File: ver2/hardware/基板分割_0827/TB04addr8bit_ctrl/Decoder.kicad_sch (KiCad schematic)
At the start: 12 parts, among them U701 74LS273, U702 74LS273, U703 28C256, U704 28C256, U705 74LS273, U706 28C256

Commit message: ver2: 3分割で他基板側のICを削除(ctrl 9・alu 15・if 2個)
削除前にまたぎ本数(37/20)で割り当てを検算。kicad-cliのパース通過を確認。

Co-Authored-By: Claude Opus 5 <noreply@anthropic.com>
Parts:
- removed U702: 74LS273, Package_DIP:DIP-20_W7.62mm_Socket, symbol 74xx:74LS273
- removed U704: 28C256, Package_DIP:DIP-28_W15.24mm_Socket, symbol Memory_EEPROM:28C256

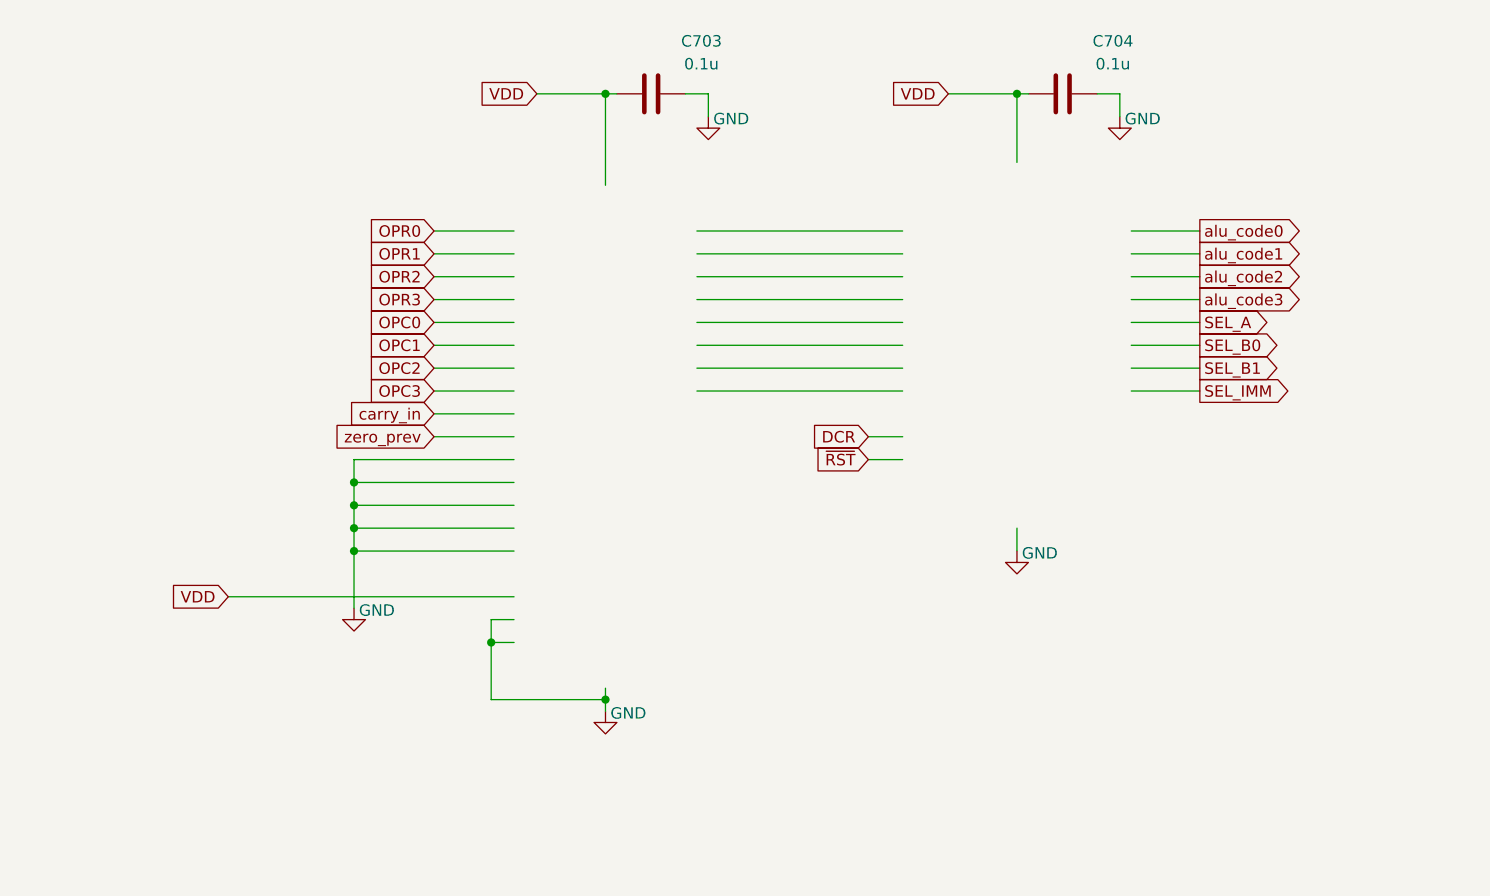
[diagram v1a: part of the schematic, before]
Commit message: ver2: 3分割でシート内の不要部品・配線を削除(検証合格)／キャリアを0827へコピー
- 制御34・演算25・IF10=IC69でマスターと一致、部品の取りこぼし0
- ピン-ネット署名の変化0件=誤って線を切った箇所なし
- またぐ信号は制御/演算35・IF/制御18で手順書の表と過不足ゼロ

Co-Authored-By: Claude Opus 5 <noreply@anthropic.com>
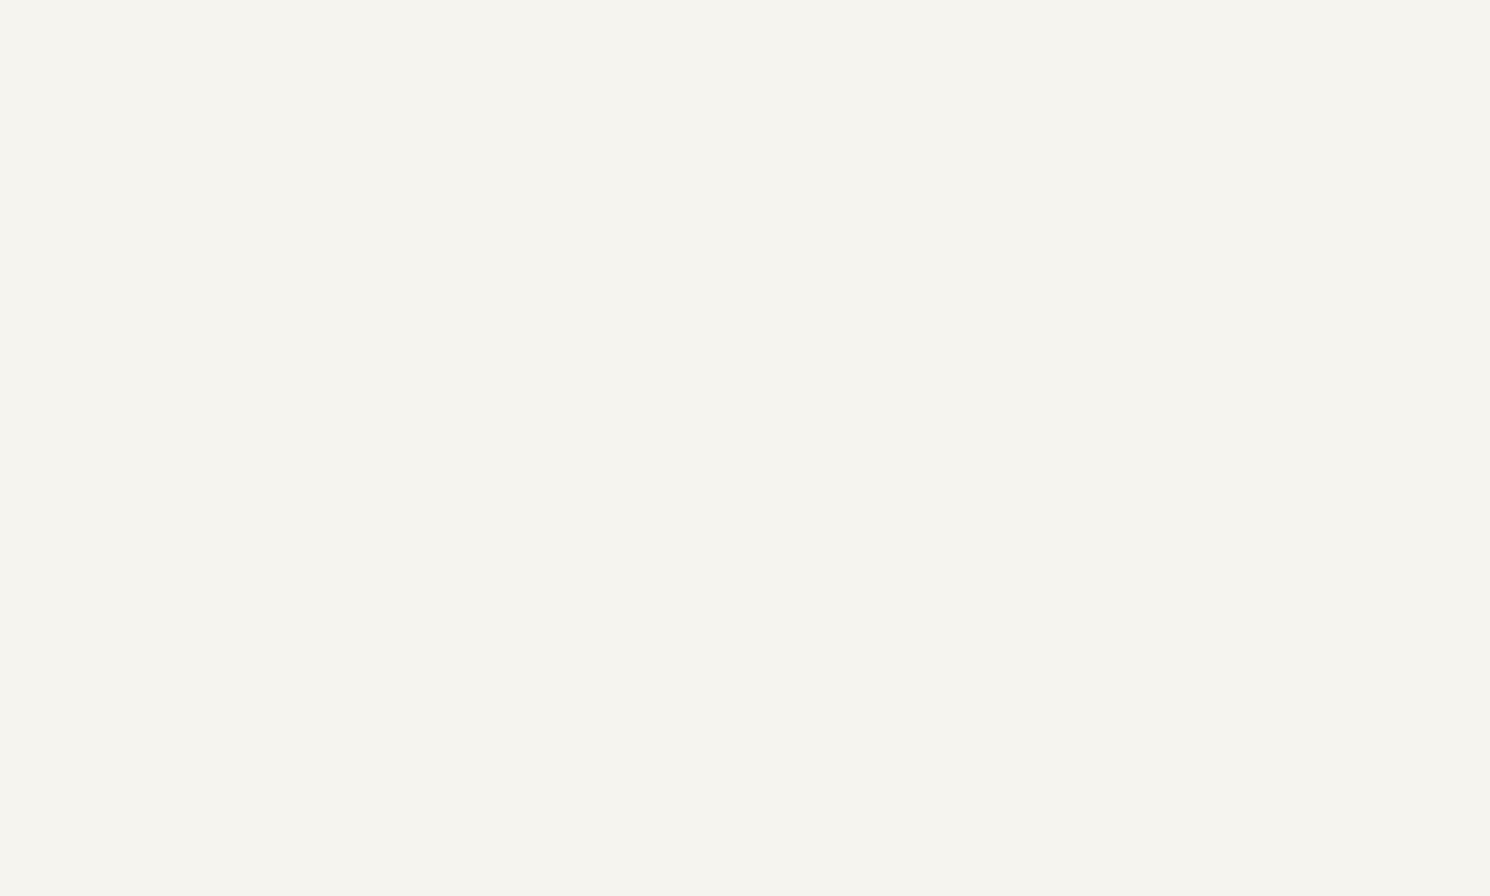
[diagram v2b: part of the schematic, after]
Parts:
- removed C703, C704: 0.1u, Capacitor_THT:C_Disc_D4.3mm_W1.9mm_P5.00mm, symbol Device:C

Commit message: ver2: 3分割の74LS表記をHCへ一括変更(31パッケージ・Valueのみ)
- 書き換えたのはValueプロパティのみ(56件=31パッケージ)
- lib_id(74xx:74LS***)とDatasheetは変更せず。HC品のシンボルがKiCADに
  無いため、lib_idを変えるとシンボル未検出になる
- 74LS->74HCの単純置換で9品種すべて実在の型番(00/08/10/32/139/157/
  253/273/377)。ピン配置は同一でネットリストへの影響なし

検証: 残存する74LSのValue 0件、git diffの変更行はValueの56行のみ
申し送り: PCB側のValueは未同期。「回路図からPCBを更新」で解消する

Co-Authored-By: Claude Opus 5 <noreply@anthropic.com>
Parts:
- U701, U705: value 74LS273 -> 74HC273
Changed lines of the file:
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@@
 			)
 		)
-		(property "Value" "74LS273"
+		(property "Value" "74HC273"
 			(at 149.4633 154.94 0)
 			(show_name no)
@@
 			)
 		)
-		(property "Value" "74LS273"
+		(property "Value" "74HC273"
 			(at 310.7533 54.61 0)
 			(show_name no)

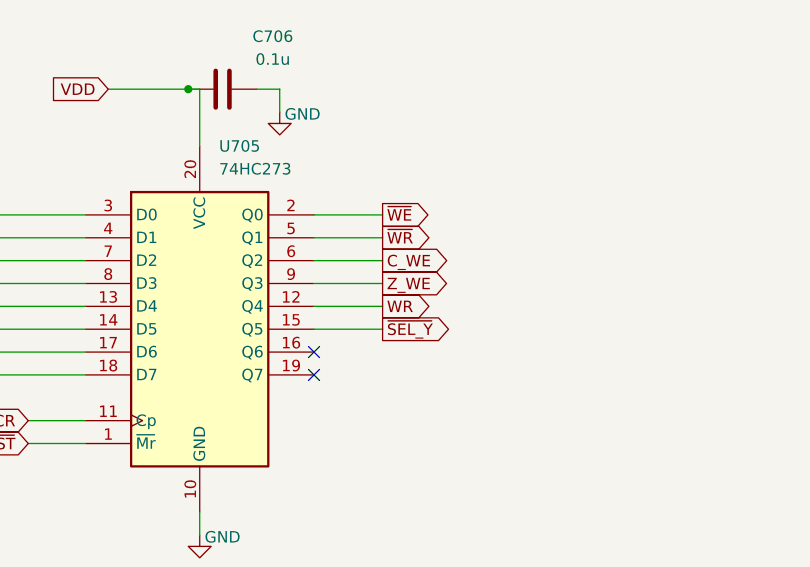
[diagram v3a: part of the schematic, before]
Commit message: ver2: シート15のゲートを6パッケージに整理(74HC08を1枚削除)
~OE_RAM を WR 直結にし(6116は /CE で出力がゲートされるため)、
RAM_STK_SEL と CS_RAM を ~CS_RAM=NAND3(P2,~P5,EXE) 1個にまとめ、
WR_EXE を NAND+INV に置き換えて AND 4つを U1503 へ集約。
U1507(74HC08)と C1502 を削除。7パッケージ27ゲート→6パッケージ25ゲート。

検証=HEADとのパッド-ネット署名比較で変化27パッド・部品103→101・
増えたネットなし・回路図↔PCBの不整合0。PCBはネットリスト同期済み。

Co-Authored-By: Claude Opus 5 <noreply@anthropic.com>
Claude-Session: https://claude.ai/code/session_012fBwfnqwV8TxUeD3onaDK6
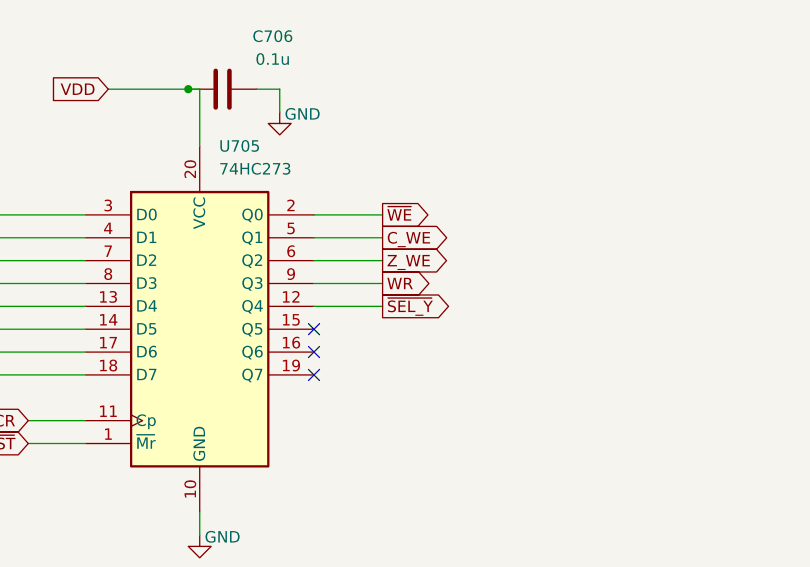
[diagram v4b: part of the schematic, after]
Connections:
- net ~{WR} is gone; now on net C_WE: U705.5 (Q1)
- net C_WE: no longer U705.6 (Q2)
- net WR: now also U705.9 (Q3); no longer U705.12 (Q4)
- net Z_WE: now also U705.6 (Q2); no longer U705.9 (Q3)
- net ~{SEL_Y}: now also U705.12 (Q4); no longer U705.15 (Q5)
- no-connect marks 2 -> 3
